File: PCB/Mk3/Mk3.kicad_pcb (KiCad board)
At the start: 2 copper layers, 42 parts, among them J1 Screw_Terminal_01x02, J10 Con12-PortA, J2 Con4-Bank, J3 Conn_01x06_Pin, J4 Con12-PortB, J5 Conn_01x32, J6 Conn_01x32, J7 Conn_01x32, J8 Conn_01x32, J9 COM: Gnd,CTS, Vcc, Tx, Rx, DTR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

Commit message: 3d model and moved trim pot
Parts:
- RV1: footprint Potentiometer_THT:Potentiometer_Runtron_RM-065_Vertical -> Potentiometer_THT:Potentiometer_Piher_PT-15-V15_Vertical
- SW1: footprint Library:MiniSwitch -> Button_Switch_THT:SW_PUSH_1P1T_6x3.5mm_H4.3_APEM_MJTP1243
- moved RV1 145.0 mm to (213.3, 166.1)
- moved C16 67.5 mm to (162.6, 166.3), turned to 90 degrees
- moved J10 66.3 mm to (157.5, 163.8)
- moved LCD1 63.8 mm to (193.0, 57.1)
- moved C18 63.8 mm to (68.6, 120.6)
- moved J3 63.8 mm to (86.4, 57.1)
- moved U5 63.8 mm to (68.6, 148.6)
- moved Y25 63.8 mm to (82.5, 34.3)
- moved C11 63.8 mm to (53.3, 21.6)
- moved U1 63.8 mm to (48.3, 27.6)
- moved C1 63.8 mm to (45.7, 33.2)
- moved C13 63.8 mm to (114.4, 21.6)
- moved C14 63.8 mm to (81.3, 69.8)
- moved C25 63.8 mm to (137.2, 21.6)
- moved C26 63.8 mm to (149.9, 21.6)
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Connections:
- J5 pad 2: /Clk2 -> /~{WR}
- J5 pad 3: /R~{W} -> /~{RD}
- J5 pad 4: /~{WR} -> /R~{W}
- J5 pad 5: /~{RD} -> /~{RST}
- J5 pad 6: /~{IRQ} -> /RDY
- J5 pad 7: /~{NMI} -> /Clk2
- J5 pad 8: /RDY -> /~{IRQ}
- J5 pad 9: /~{RST} -> /~{NMI}
- J6 pad 2: /Clk2 -> /~{WR}
- J6 pad 3: /R~{W} -> /~{RD}
- J6 pad 4: /~{WR} -> /R~{W}
- J6 pad 5: /~{RD} -> /~{RST}
- J6 pad 6: /~{IRQ} -> /RDY
- J6 pad 7: /~{NMI} -> /Clk2
- J6 pad 8: /RDY -> /~{IRQ}
- J6 pad 9: /~{RST} -> /~{NMI}
- J7 pad 2: /Clk2 -> /~{WR}
- J7 pad 3: /R~{W} -> /~{RD}
- J7 pad 4: /~{WR} -> /R~{W}
- J7 pad 5: /~{RD} -> /~{RST}
- J7 pad 6: /~{IRQ} -> /RDY
- J7 pad 7: /~{NMI} -> /Clk2
- J7 pad 8: /RDY -> /~{IRQ}
- J7 pad 9: /~{RST} -> /~{NMI}
- J8 pad 2: /Clk2 -> /~{WR}
- J8 pad 3: /R~{W} -> /~{RD}
- J8 pad 4: /~{WR} -> /R~{W}
- J8 pad 5: /~{RD} -> /~{RST}
- J8 pad 6: /~{IRQ} -> /RDY
- J8 pad 7: /~{NMI} -> /Clk2
- J8 pad 8: /RDY -> /~{IRQ}
- J8 pad 9: /~{RST} -> /~{NMI}
- U3 pad 11: unconnected-(U3-In10-Pad11) -> /Clk2
- U3 pad 6: /Clk2 -> unconnected-(U3-In05-Pad6)
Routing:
- net Net-(LCD1-V0): track 12.9 -> 131.3 mm
- net /~{RST}: track 274.7 -> 371.4 mm, vias 0 -> 2
- net +5V: track 762.2 -> 850.3 mm, vias 14 -> 16
- net GND: track 1107.9 -> 1185.9 mm
- net Net-(LCD1-VOUT): track 47.4 -> 110.2 mm
- net /R~{W}: track 287.5 -> 248.0 mm, vias 8 -> 6
- net /DISP: track 138.4 -> 104.3 mm, vias 0 -> 2
- net /Clk2: track 348.1 -> 323.1 mm
- net /~{IRQ}: track 213.4 -> 200.7 mm
- net /D0: track 485.2 -> 473.4 mm
- net /D2: track 487.6 -> 476.6 mm
- net /D1: track 486.9 -> 475.8 mm
- net /D3: track 508.4 -> 497.3 mm
- net /D4: track 473.3 -> 465.3 mm
- net /~{RD}: track 253.1 -> 260.2 mm, vias 4 -> 2
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
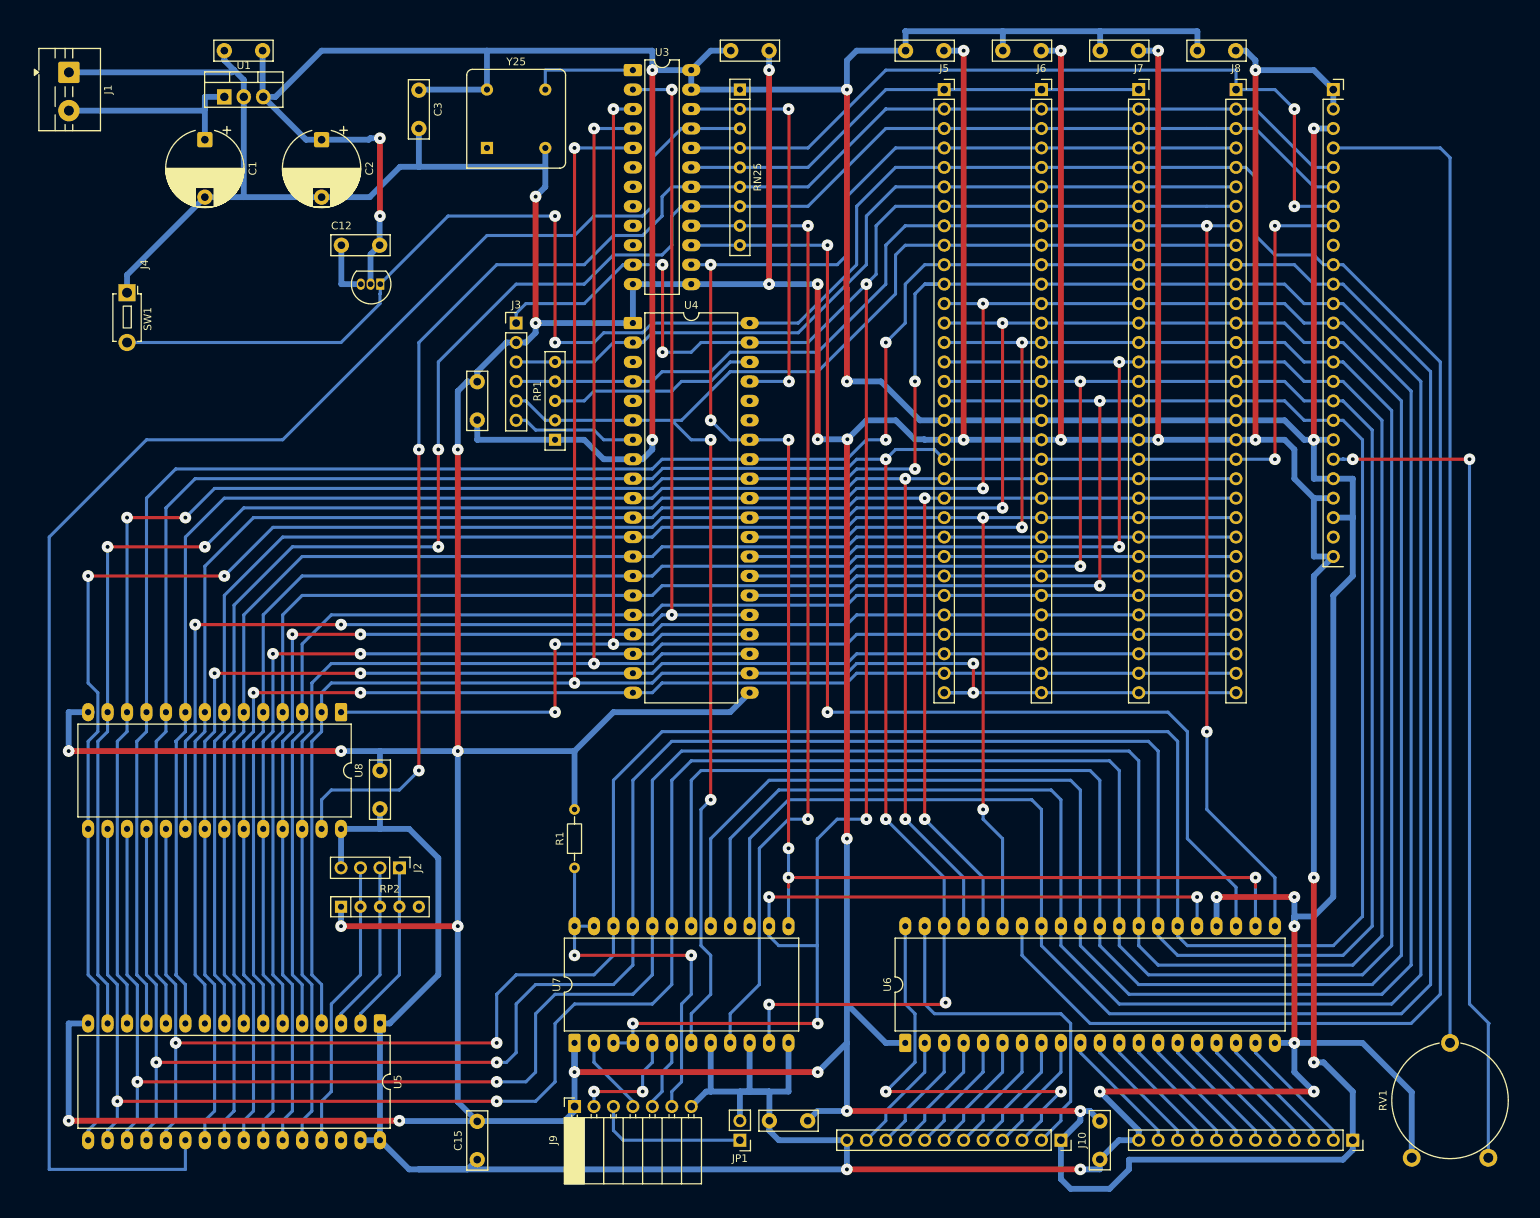
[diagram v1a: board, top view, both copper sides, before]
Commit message: updated silk & foot prints
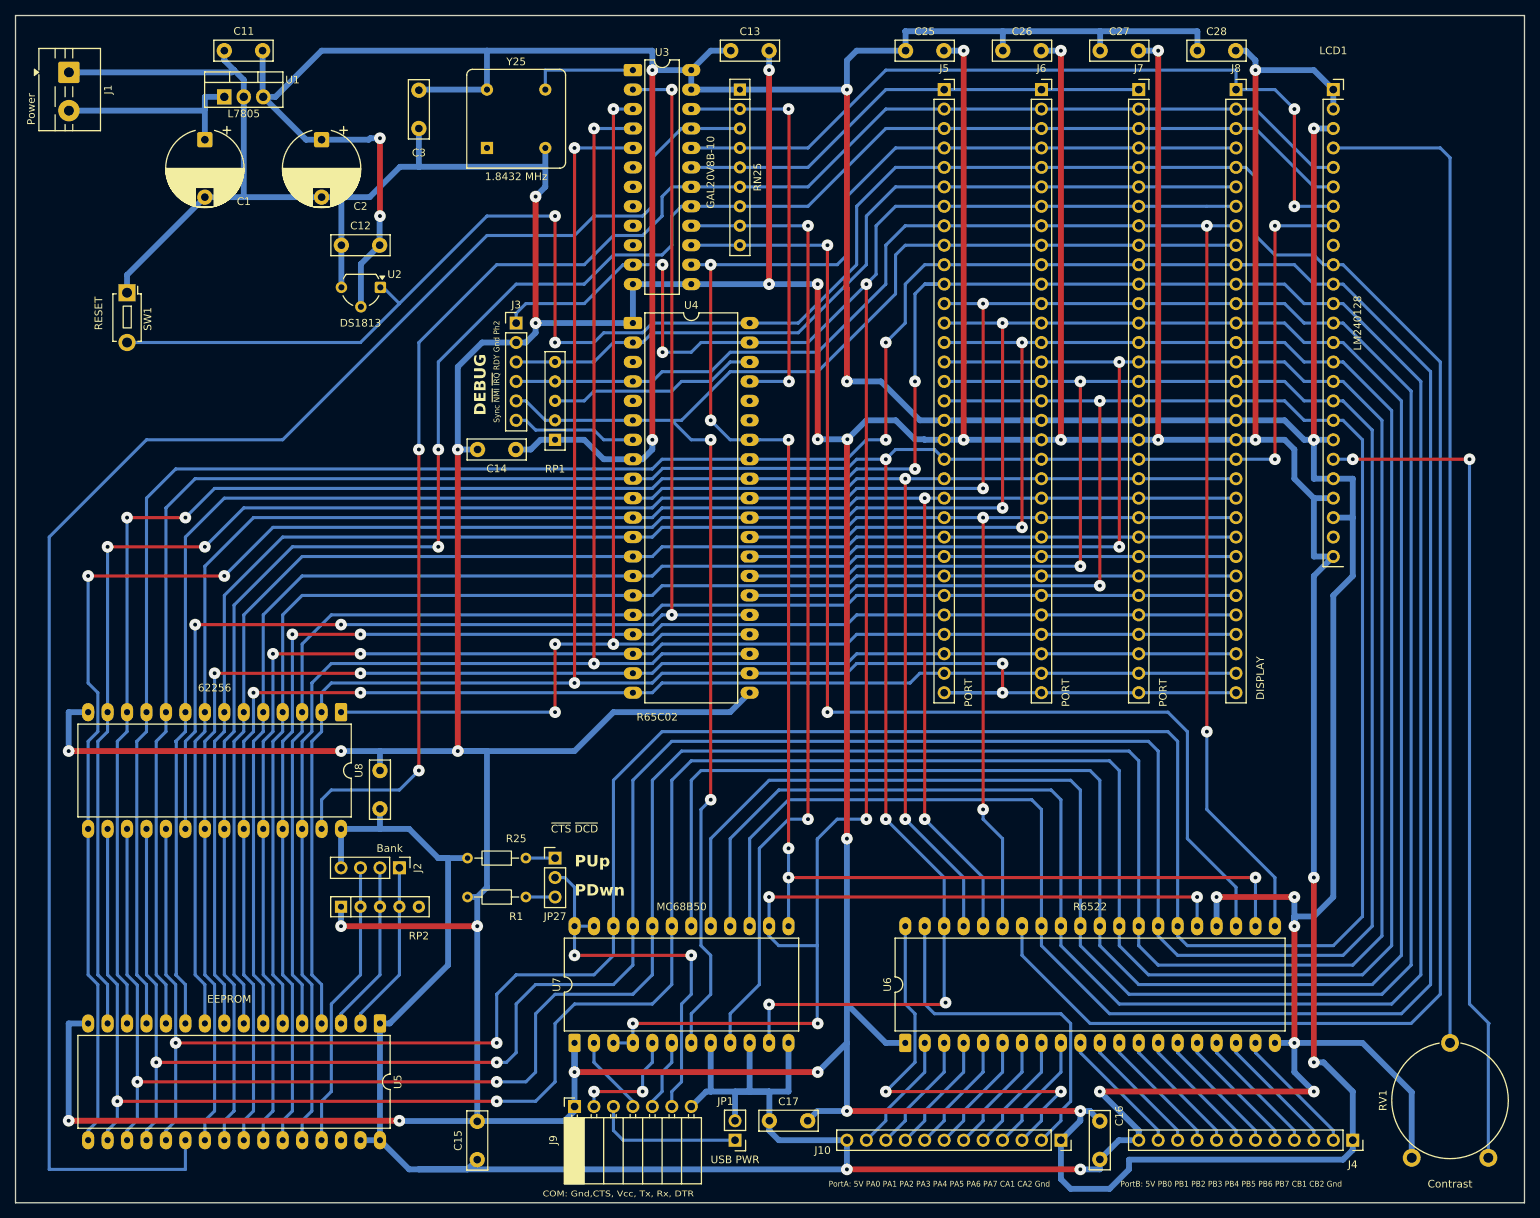
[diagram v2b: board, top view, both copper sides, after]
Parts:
- added JP27: ~{CTS} ~{DCD}, Connector_PinHeader_2.54mm:PinHeader_1x03_P2.54mm_Vertical, F.Cu at (91.4, 127.0)
- added R25: PUp, Resistor_THT:R_Axial_DIN0204_L3.6mm_D1.6mm_P7.62mm_Horizontal, F.Cu at (87.6, 127.0)
- J1: value Screw_Terminal_01x02 -> Power
- J10: value Con12-PortA -> PortA: 5V PA0 PA1 PA2 PA3 PA4 PA5 PA6 PA7 CA1 CA2 Gnd
- J2: value Con4-Bank -> Bank
- J3: value Conn_01x06_Pin -> Sync ~{NMI} ~{IRQ} RDY Gnd Ph2
- J4: value Con12-PortB -> PortB: 5V PB0 PB1 PB2 PB3 PB4 PB5 PB6 PB7 CB1 CB2 Gnd
- J5, J6, J7: value Conn_01x32 -> PORT
- J8: value Conn_01x32 -> DISPLAY
- JP1: value Jumper_2_Open -> USB PWR
- R1: value R_Small_US -> PDwn
- RV1: value R_Trim -> Contrast
- SW1: value SW_Push -> RESET
- U2: footprint Package_TO_SOT_THT:TO-92L_Inline -> Package_TO_SOT_THT:TO-92L_Wide
- Y25: value CXO_DIP8 -> 1.8432 MHz
- moved R1 7.41 mm to (87.6, 132.1), turned to 180 degrees
- moved C14 6.34 mm to (86.3, 73.7), turned to 180 degrees
- moved JP1 0.63 mm to (114.9, 163.8)
- moved U2 0.42 mm to (68.6, 52.5)
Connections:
- net Net-(J10-Pin_10) renamed /PA1
- net Net-(J10-Pin_11) renamed /PA0
- net Net-(J10-Pin_2) renamed /CA2
- net Net-(J10-Pin_3) renamed /CA1
- net Net-(J10-Pin_4) renamed /PA7
- net Net-(J10-Pin_5) renamed /PA6
- net Net-(J10-Pin_6) renamed /PA5
- net Net-(J10-Pin_7) renamed /PA4
- net Net-(J10-Pin_8) renamed /PA3
- net Net-(J10-Pin_9) renamed /PA2
- net Net-(J4-Pin_10) renamed /PB1
- net Net-(J4-Pin_11) renamed /PB0
- net Net-(J4-Pin_2) renamed /CB2
- net Net-(J4-Pin_3) renamed /CB1
- net Net-(J4-Pin_4) renamed /PB7
- net Net-(J4-Pin_5) renamed /PB6
- net Net-(J4-Pin_6) renamed /PB5
- net Net-(J4-Pin_7) renamed /PB4
- net Net-(J4-Pin_8) renamed /PB3
- net Net-(J4-Pin_9) renamed /PB2
- R1 pad 1: Net-(J9-Pin_6) -> Net-(JP27-B)
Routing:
- net /A12: track 254.1 -> 261.7 mm
- net GND: track 1185.9 -> 1192.8 mm
- net Net-(JP27-B): track 0.00 -> 3.81 mm
- net Net-(JP27-A): track 0.00 -> 3.81 mm
- net +5V: track 850.3 -> 852.9 mm
- net /R~{W}: track 248.0 -> 245.5 mm
- net /~{RST}: track 371.4 -> 373.3 mm
- net Net-(J9-Pin_3): track 20.2 -> 19.5 mm
- net Net-(J9-Pin_6): track 50.0 -> 50.5 mm
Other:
- board outline added: 197 x 155 mm
- board text added: "DEBUG"
- board text added: "PDwn"
- board text added: "PUp"

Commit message: save
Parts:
- added R26: R_Small_US, Resistor_THT:R_Axial_DIN0204_L3.6mm_D1.6mm_P7.62mm_Horizontal, F.Cu at (81.3, 66.0)
- moved C3 27.8 mm to (99.1, 38.1)
- moved C14 25.6 mm to (109.2, 85.1)
- moved U6 25.6 mm to (160.0, 162.6)
- moved C13 25.6 mm to (137.2, 33.0)
- moved C25 25.6 mm to (160.1, 33.0)
- moved C27 25.6 mm to (185.5, 33.0)
- moved J6 25.6 mm to (177.8, 38.1)
- moved J7 25.6 mm to (190.5, 38.1)
- moved LCD1 25.6 mm to (215.9, 68.6)
- moved RN25 25.6 mm to (138.4, 38.1)
- moved C11 25.6 mm to (76.1, 33.0)
- moved C15 25.6 mm to (104.1, 177.8)
- moved C17 25.6 mm to (142.3, 172.7)
- moved C18 25.6 mm to (91.4, 132.0)
- moved J1 25.6 mm to (50.8, 35.9)
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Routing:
- net +5V: track 852.9 -> 858.2 mm
- net /~{RST}: track 373.3 -> 378.4 mm
- net GND: track 1192.8 -> 1195.4 mm
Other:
- board text added: "Anton's Retro 6502"

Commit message: Save point
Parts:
- removed C27: C, Capacitor_THT:C_Disc_D7.5mm_W2.5mm_P5.00mm
- removed J7: PORT, Connector_PinSocket_2.54mm:PinSocket_1x32_P2.54mm_Vertical
- J5: value PORT -> DISPLAY
- J8: value DISPLAY -> PORT
- moved R26 34.2 mm to (94.0, 34.3), turned to -90 degrees
- moved C15 28.4 mm to (99.1, 149.9), turned to 0 degrees
- moved C12 21.3 mm to (91.2, 37.1)
- moved U2 21.3 mm to (91.3, 42.6)
- moved C2 7.62 mm to (76.2, 44.6)
- moved J6 6.35 mm to (184.2, 38.1)
- moved C26 6.31 mm to (179.1, 33.0)
- moved C1 5.72 mm to (62.9, 44.5)
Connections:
- J5 pad 1: /~{PORT} -> /DISP
- J8 pad 1: /DISP -> /~{PORT}
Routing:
- net GND: track 1195.4 -> 1095.2 mm, vias 30 -> 29
- net +5V: track 858.2 -> 820.4 mm
- net /~{RST}: track 378.4 -> 407.0 mm
- net /D7: track 447.9 -> 473.5 mm, vias 4 -> 2
- net /D6: track 454.1 -> 478.9 mm, vias 4 -> 2
- net /D5: track 471.4 -> 494.0 mm, vias 4 -> 2
- net /Clk2: track 323.1 -> 306.0 mm
- net /D4: track 465.3 -> 481.9 mm, vias 4 -> 2
- net Net-(J9-Pin_2): track 15.2 -> 29.2 mm, vias 2 -> 0
- net /~{PORT}: track 62.6 -> 75.3 mm
- net /~{ROM}: track 220.1 -> 211.4 mm, vias 0 -> 2
- net /R~{W}: track 245.5 -> 253.1 mm
- net /PWR: track 26.0 -> 29.3 mm
- net /DISP: track 104.3 -> 101.3 mm
- net /A1: track 266.5 -> 268.4 mm
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
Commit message: Latest variation
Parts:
- removed R1: PDwn, Resistor_THT:R_Axial_DIN0204_L3.6mm_D1.6mm_P7.62mm_Horizontal
- added JP25: LOROM, Connector_PinHeader_2.54mm:PinHeader_1x02_P2.54mm_Vertical, F.Cu at (86.4, 144.8)
- added JP26: L-ROM-H, Connector_PinHeader_2.54mm:PinHeader_1x03_P2.54mm_Vertical, F.Cu at (105.4, 134.0)
- added JP28: A13R, Jumper:SolderJumper-2_P1.3mm_Bridged_RoundedPad1.0x1.5mm, F.Cu at (88.9, 141.6)
- JP27: value ~{CTS} ~{DCD} -> L-~{CTS} ~{DCD}-H
- moved C15 14.9 mm to (104.1, 163.9), turned to -90 degrees
- moved JP27 13.7 mm to (102.9, 146.1)
- moved J2 12.2 mm to (86.4, 149.2), turned to 90 degrees
- moved R25 5.85 mm to (109.2, 144.1), turned to 0 degrees
- moved RP2 5.72 mm to (86.4, 139.1)
- moved J1 2.76 mm to (51.1, 33.1)
- moved U5 2.54 mm to (88.9, 160.0)
- moved R26 1.27 mm to (95.2, 34.3)
- moved C12 1.00 mm to (91.4, 38.1)
- moved U1 0.96 mm to (71.1, 40.0)
- moved U2 0.33 mm to (91.5, 42.3)
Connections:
- J2 pad 1: /BA3 -> /BA0
- J2 pad 2: /BA2 -> /BA1
- J2 pad 3: /BA1 -> /BA2
- J2 pad 4: +5V -> /BA3
- JP27 pad 1: Net-(JP27-A) -> +5V
- JP27 pad 2: Net-(J9-Pin_6) -> Net-(JP27-C)
- JP27 pad 3: Net-(JP27-B) -> GND
- R25 pad 1: Net-(JP27-A) -> Net-(JP27-C)
- R25 pad 2: +5V -> Net-(J9-Pin_6)
- RP2 pad 1: GND -> Net-(JP26-C)
- RP2 pad 2: /BA1 -> Net-(JP28-B)
- RP2 pad 3: /BA2 -> /BA1
- RP2 pad 4: /BA3 -> /BA2
- RP2 pad 5: unconnected-(RP2-R4-Pad5) -> /BA3
- U5 pad 28: /A13 -> /BA0
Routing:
- net GND: track 1095.2 -> 1135.7 mm, vias 29 -> 26
- net /BA0: track 0.00 -> 37.9 mm
- net /BA1: track 37.7 -> 66.3 mm
- net /A13: track 194.9 -> 167.5 mm, vias 2 -> 5
- net Net-(JP26-C): track 0.00 -> 21.5 mm, vias 0 -> 2
- net +5V: track 820.4 -> 837.7 mm
- net Net-(JP27-C): track 0.00 -> 9.68 mm
- net Net-(LCD1-V0): track 131.3 -> 124.6 mm
- net Net-(J9-Pin_6): track 50.5 -> 45.5 mm
- net /PWR: track 29.3 -> 24.5 mm
- net /BA3: track 22.4 -> 27.1 mm
- net /BA2: track 22.4 -> 26.4 mm
- net Net-(JP27-B): track 3.81 -> 0.00 mm
- net Net-(JP27-A): track 3.81 -> 0.00 mm
- net /D1: track 475.8 -> 472.2 mm
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- added copper zone on B.Cu, net GND
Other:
- board size 197 x 155 mm -> 197 x 157.5 mm
- board text added: "PCB Stock is 197 x 253"
- board text removed: "PDwn"
- board text removed: "PUp"
